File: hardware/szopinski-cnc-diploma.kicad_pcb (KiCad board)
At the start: 4 copper layers, 99.1 x 55.9 mm, 26 parts, among them J1 Barrel_Jack, J2 Conn_02x08_Odd_Even, J3 AVR-ISP-10, J4 Conn_01x04, J5 Conn_01x04, J6 Conn_01x04, J7 Conn_01x04, U1 ATmega328P-PU, U2 L7805, U3 DRV8825, U4 DRV8825, U5 DRV8825, U6 DRV8825, Y1 20 MHz

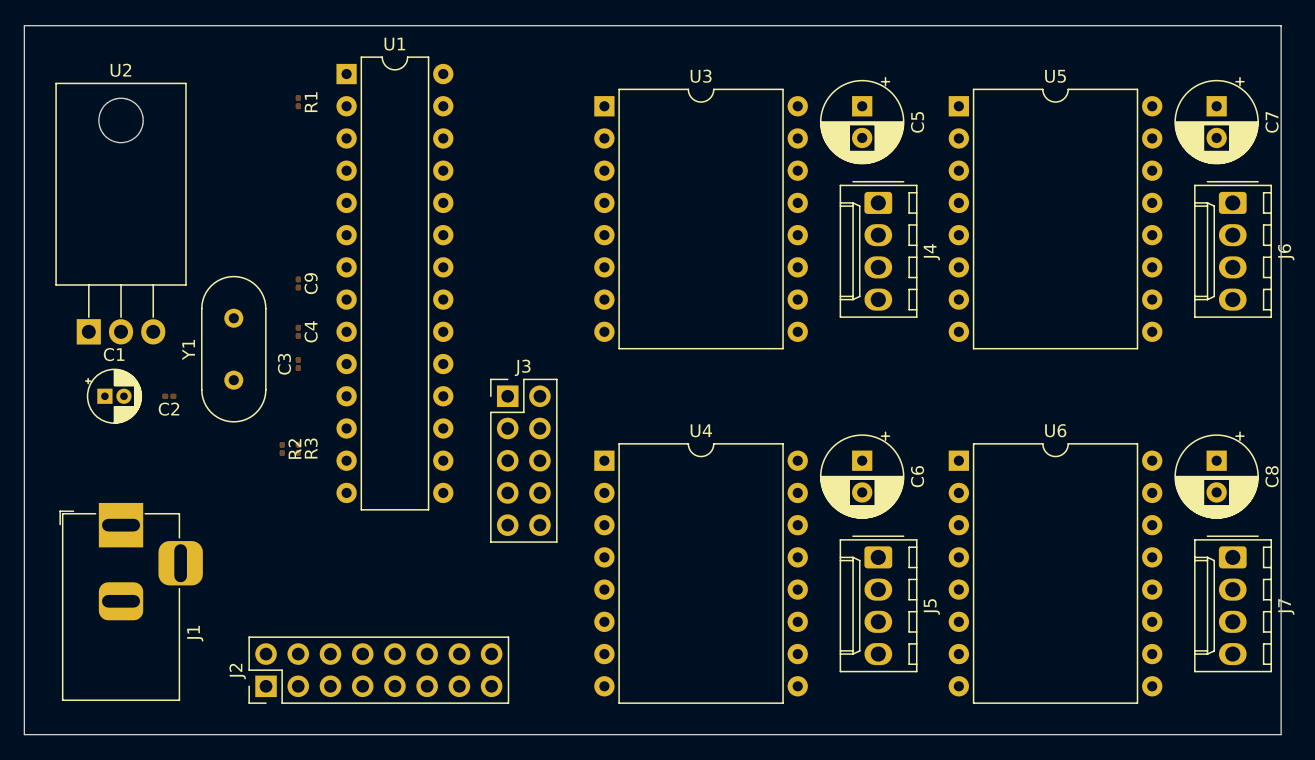
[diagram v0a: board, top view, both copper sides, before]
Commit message: Add traces
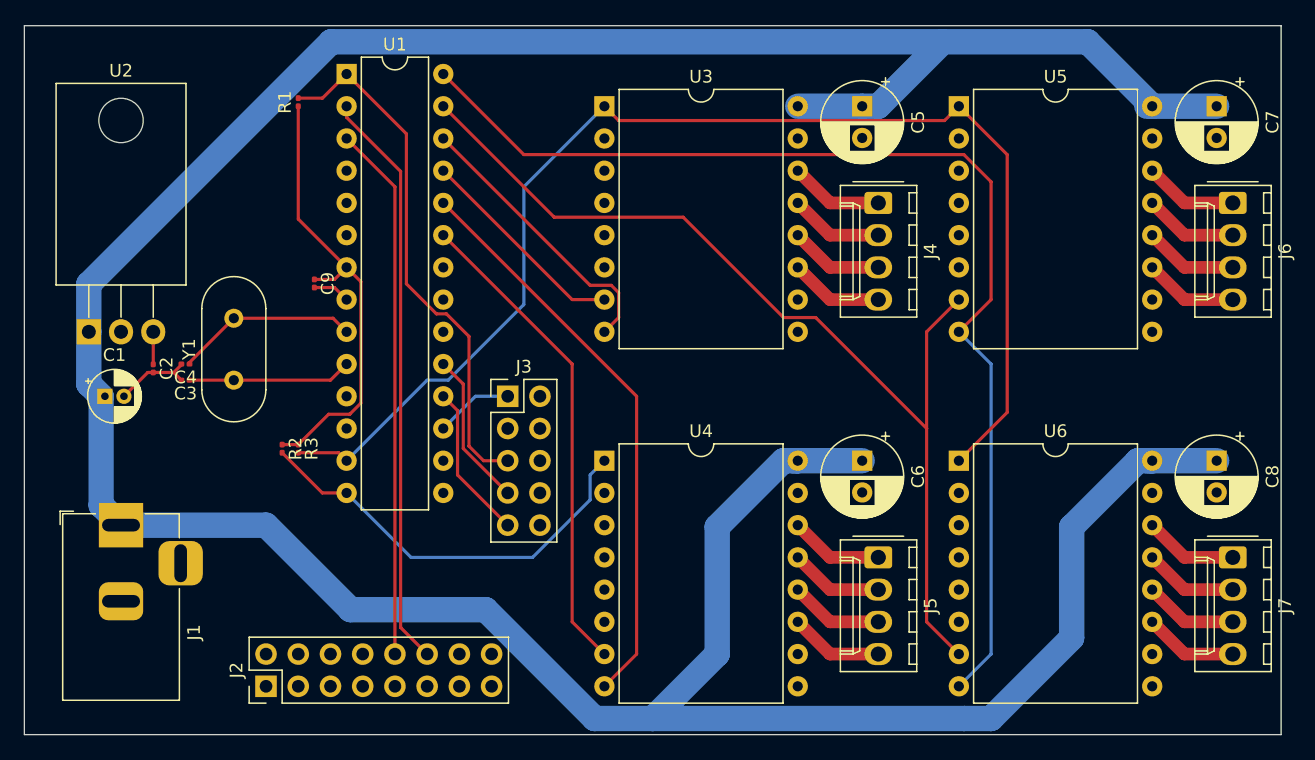
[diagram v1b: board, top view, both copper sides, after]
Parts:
- moved C4 9.25 mm to (86.4, 72.4), turned to 180 degrees
- moved C3 8.98 mm to (86.4, 73.7), turned to 180 degrees
- moved C2 2.54 mm to (83.8, 72.7), turned to 270 degrees
- moved C9 1.27 mm to (96.5, 66.0)
- turned R1 to 90 degrees
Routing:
- net +15V: track 0.00 -> 270.8 mm
- net /ENABLE_XY: track 0.00 -> 101.4 mm
- net /DIR_Y: track 0.00 -> 89.6 mm
- net /STEP_Y: track 0.00 -> 78.7 mm
- net /RXD: track 0.00 -> 45.8 mm
- net /DIR_Z: track 0.00 -> 45.5 mm
- net /TXD: track 0.00 -> 42.2 mm
- net /RESET: track 0.00 -> 41.9 mm
- net +5V: track 0.00 -> 38.5 mm
- net /STEP_Z: track 0.00 -> 38.3 mm
- net /ENABLE_Z: track 0.00 -> 33.1 mm
- net /DIR_X: track 0.00 -> 22.4 mm
- net /STEP_X: track 0.00 -> 16.9 mm
- net Net-(C4-Pad1): track 0.00 -> 14.8 mm
- net Net-(C3-Pad1): track 0.00 -> 13.4 mm
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
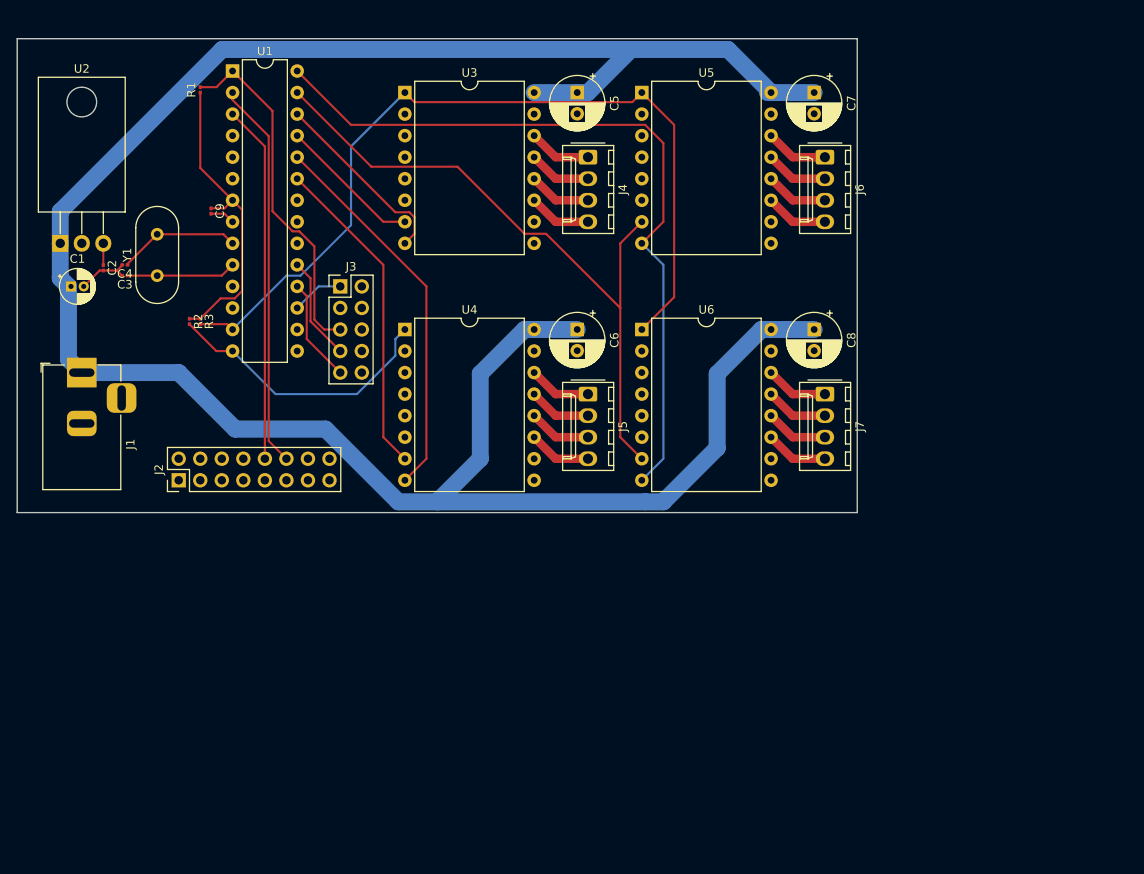
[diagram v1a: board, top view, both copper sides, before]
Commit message: Fix footprints, symbols and clearance issues
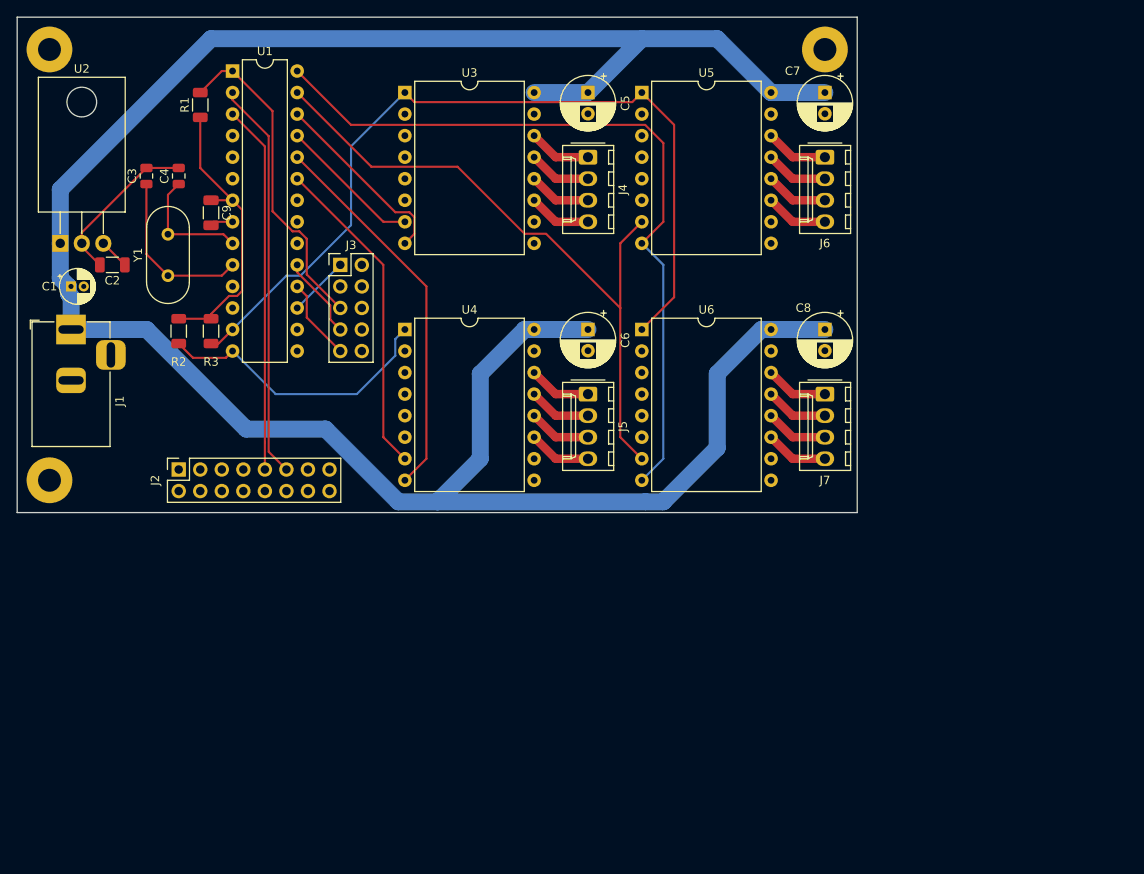
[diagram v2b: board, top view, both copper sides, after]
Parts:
- added REF**: MountingHole_2.7mm_Pad, MountingHole:MountingHole_2.7mm_Pad, F.Cu at (77.5, 47.0)
- added REF**: MountingHole_2.7mm_Pad, MountingHole:MountingHole_2.7mm_Pad, F.Cu at (168.9, 47.0)
- added REF**: MountingHole_2.7mm_Pad, MountingHole:MountingHole_2.7mm_Pad, F.Cu at (77.5, 97.8)
- C2, C9: footprint Capacitor_SMD:C_0201_0603Metric -> Capacitor_SMD:C_1206_3216Metric
- C3, C4: footprint Capacitor_SMD:C_0201_0603Metric -> Capacitor_SMD:C_0805_2012Metric
- J2: footprint Connector_PinHeader_2.54mm:PinHeader_2x08_P2.54mm_Vertical -> Connector_PinSocket_2.54mm:PinSocket_2x08_P2.54mm_Vertical
- R1, R2, R3: footprint Resistor_SMD:R_0201_0603Metric -> Resistor_SMD:R_1206_3216Metric
- moved C4 12.3 mm to (92.7, 61.9), turned to 90 degrees
- moved C3 12.0 mm to (88.9, 61.9), turned to 90 degrees
- moved J1 5.24 mm to (80.0, 80.0)
- moved J3 2.54 mm to (111.8, 72.4)
- moved R1 1.78 mm to (95.2, 53.5)
- moved R2 1.71 mm to (92.7, 80.2)
- moved R3 1.71 mm to (96.5, 80.2)
- moved C5 1.27 mm to (141.0, 52.1)
- moved C6 1.27 mm to (141.0, 80.0)
- moved C7 1.27 mm to (168.9, 52.1)
- moved C8 1.27 mm to (168.9, 80.0)
- moved J2 1.27 mm to (92.7, 96.5)
- moved Y1 1.27 mm to (91.4, 73.7)
- moved C2 1.12 mm to (84.9, 72.4), turned to 180 degrees
- moved C9 0.20 mm to (96.5, 66.2)
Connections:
- net +15V renamed +18V
- J2 pad 1: +5V -> Net-(J2-Pad1)
- J2 pad 10: /TXD -> Net-(J2-Pad10)
- J2 pad 11: Net-(J2-Pad11) -> /RXD
- J2 pad 12: /RXD -> Net-(J2-Pad12)
- J2 pad 15: Net-(J2-Pad15) -> GND
- J2 pad 16: GND -> Net-(J2-Pad16)
- J2 pad 2: Net-(J2-Pad2) -> +5V
- J2 pad 9: Net-(J2-Pad9) -> /TXD
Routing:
- net GND: track 9.41 -> 22.0 mm
- net Net-(C3-Pad1): track 13.4 -> 20.5 mm
- net +18V: track 270.8 -> 276.3 mm
- net /RESET: track 41.9 -> 38.5 mm
- net Net-(J3-Pad9): track 12.3 -> 9.72 mm
- net Net-(J3-Pad7): track 12.3 -> 9.72 mm
- net /TXD: track 42.2 -> 43.5 mm
- net /RXD: track 45.8 -> 47.1 mm
- net Net-(J3-Pad1): track 6.13 -> 7.18 mm
- net /ENABLE_Z: track 33.1 -> 34.1 mm
- net /ENABLE_XY: track 101.4 -> 100.5 mm
- net +5V: track 38.5 -> 37.8 mm
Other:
- board size 99.1 x 55.9 mm -> 99.1 x 58.4 mm

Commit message: Redesign PCB
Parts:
- removed the REF** at (77.5, 47.0)
- removed the REF** at (168.9, 47.0)
- removed the REF** at (77.5, 97.8)
- added REF**: MountingHole_2.7mm_Pad, MountingHole:MountingHole_2.7mm_Pad, F.Cu at (109.2, 138.4)
- added REF**: MountingHole_2.7mm_Pad, MountingHole:MountingHole_2.7mm_Pad, F.Cu at (200.7, 138.4)
- added REF**: MountingHole_2.7mm_Pad, MountingHole:MountingHole_2.7mm_Pad, F.Cu at (200.7, 83.8)
- added REF**: MountingHole_2.7mm_Pad, MountingHole:MountingHole_2.7mm_Pad, F.Cu at (109.2, 83.8)
- C2, C9: footprint Capacitor_SMD:C_1206_3216Metric -> Capacitor_THT:C_Disc_D6.0mm_W4.4mm_P5.00mm
- C3, C4: footprint Capacitor_SMD:C_0805_2012Metric -> Capacitor_THT:C_Disc_D6.0mm_W4.4mm_P5.00mm
- C5, C6, C7, C8: value CP -> 100u
- R1, R2, R3: footprint Resistor_SMD:R_1206_3216Metric -> Resistor_THT:R_Axial_DIN0207_L6.3mm_D2.5mm_P7.62mm_Horizontal
- U2: footprint Package_TO_SOT_THT:TO-220-3_Horizontal_TabDown -> Package_TO_SOT_THT:TO-220-3_Vertical
- moved R3 96.7 mm to (188.0, 111.8), turned to 180 degrees
- moved U2 82.8 mm to (133.3, 132.1), turned to 270 degrees
- moved C2 78.7 mm to (129.5, 137.2)
- moved R2 74.3 mm to (160.0, 111.8), turned to 180 degrees
- moved C1 73.8 mm to (128.3, 130.8), turned to 270 degrees
- moved C3 63.6 mm to (118.7, 118.1), turned to 180 degrees
- moved J1 62.3 mm to (119.4, 128.3), turned to 0 degrees
- moved C4 57.4 mm to (118.7, 113.0), turned to 180 degrees
- moved Y1 54.5 mm to (123.2, 117.9)
- moved R1 51.3 mm to (123.2, 96.5)
- moved U1 49.0 mm to (128.3, 88.9)
- moved J4 47.0 mm to (170.2, 96.5)
- moved J5 47.0 mm to (170.2, 124.5)
- moved J6 47.0 mm to (198.1, 96.5)
- moved J7 47.0 mm to (198.1, 124.5)
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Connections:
- U1 pad 13: /ENABLE_XY -> Net-(U1-Pad13)
- U1 pad 14: /ENABLE_Z -> Net-(U1-Pad14)
- U1 pad 15: Net-(U1-Pad15) -> /ENABLE_Z
- U1 pad 4: Net-(U1-Pad4) -> /ENABLE_XY
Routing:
- net +5V: track 37.8 -> 312.5 mm, vias 0 -> 6
- net +18V: track 276.3 -> 198.8 mm
- net /RXD: track 47.1 -> 13.5 mm, vias 0 -> 1
- net /TXD: track 43.5 -> 11.4 mm
- net GND: track 22.0 -> 0.00 mm
- net /STEP_Y: track 78.7 -> 91.4 mm, vias 0 -> 2
- net /ENABLE_Z: track 34.1 -> 23.0 mm, vias 0 -> 1
- net Net-(C3-Pad1): track 20.5 -> 13.4 mm
- net /RESET: track 38.5 -> 45.3 mm, vias 0 -> 2
- net Net-(J3-Pad1): track 7.18 -> 10.5 mm
- net Net-(C4-Pad1): track 15.0 -> 11.7 mm
- net Net-(J3-Pad7): track 9.72 -> 7.18 mm
- net Net-(J3-Pad9): track 9.72 -> 7.18 mm
- net /DIR_X: track 22.4 -> 20.2 mm, vias 0 -> 1
- net /STEP_X: track 16.9 -> 15.9 mm
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- added copper zone on B.Cu, net GND
- removed copper zone on In1.Cu, net +5V
- removed copper zone on In2.Cu, net GND
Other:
- board size 99.1 x 58.4 mm -> 99.1 x 62.2 mm
- copper layers 4 -> 2
- board text added: "A1"
- board text added: "A2"
- board text added: "B1"
- board text added: "B2"
- board text added: "CNC machine controller Michał Szopiński"
- board text added: "Center-positive 35V max"
- board text added: "FT232 breakout board"
- board text added: "GND"
- board text added: "ISP"
- board text added: "MISO"
- board text added: "MOSI"
- board text added: "RST"
- board text added: "SCK"
- board text added: "VCC"
- board text added: "X"
- board text added: "Y1"
- board text added: "Y2"
- board text added: "Z"
- board text added: "μC RX"
- board text added: "μC TX"

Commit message: Add custom symbol and footprint to project
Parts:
- U3, U4, U5, U6: footprint Package_DIP:DIP-16_W15.24mm -> szopinski-cnc-diploma:DIP-16_W15.24mm

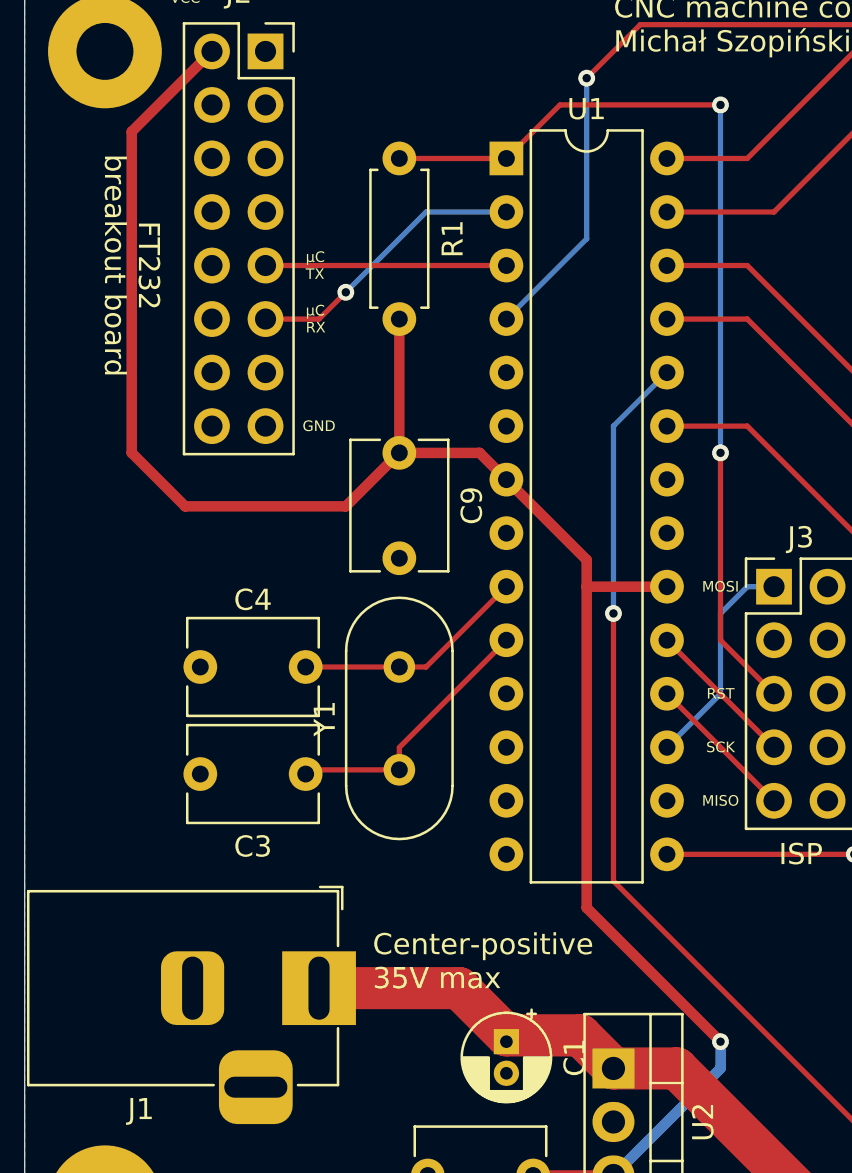
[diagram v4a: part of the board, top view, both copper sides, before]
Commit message: Reroute FT232 power
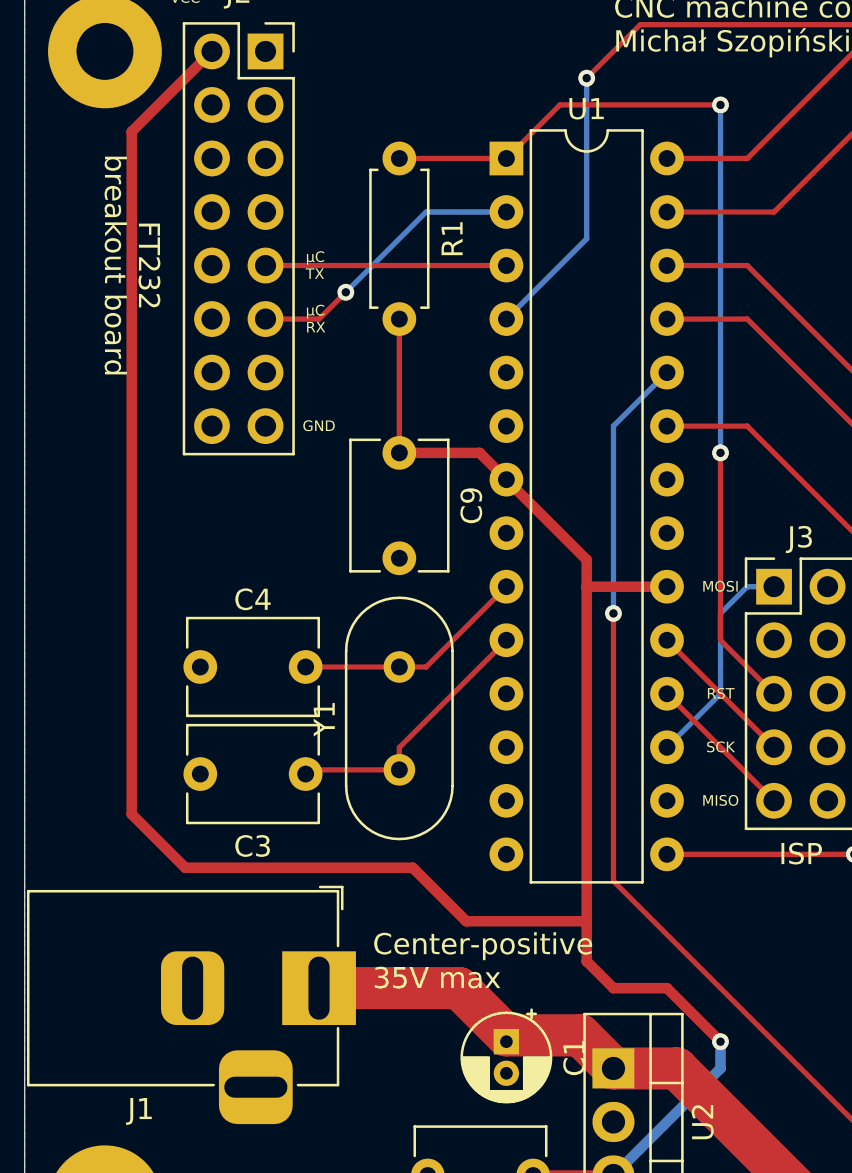
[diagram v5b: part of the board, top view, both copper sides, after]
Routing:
- net +5V: track 312.5 -> 340.0 mm

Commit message: Change 18V to 12V
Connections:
- net +18V renamed +12V

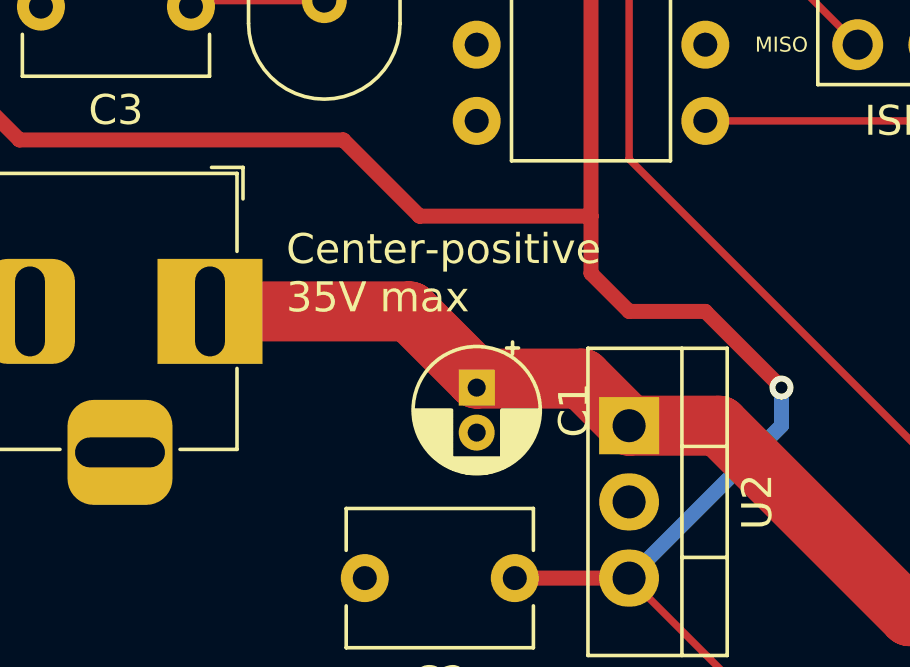
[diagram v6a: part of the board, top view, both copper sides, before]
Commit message: Increase input capacitor value
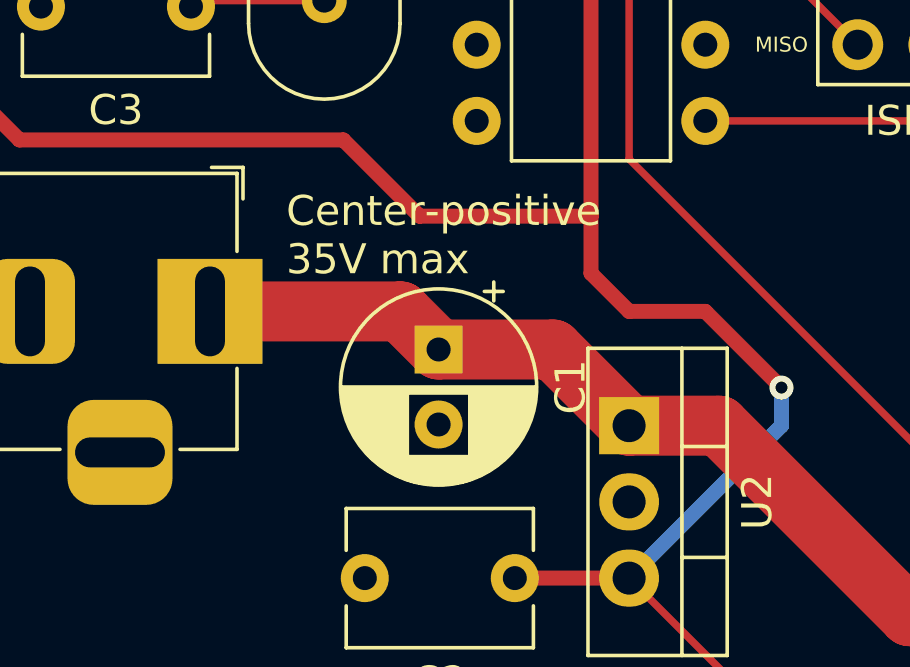
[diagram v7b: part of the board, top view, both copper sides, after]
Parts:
- C1: value 470n -> 100u; footprint Capacitor_THT:CP_Radial_D4.0mm_P1.50mm -> Capacitor_THT:CP_Radial_D6.3mm_P2.50mm
- moved C1 1.80 mm to (127.0, 129.5)
